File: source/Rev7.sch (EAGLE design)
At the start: 8 parts

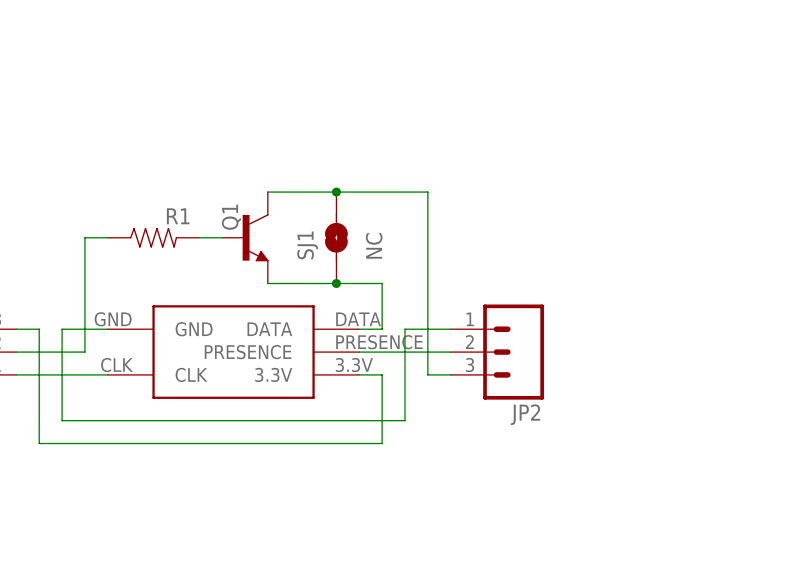
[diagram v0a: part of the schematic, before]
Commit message: Updated Rev7: down to 1 via and much better signal layout. Pin layout has changed
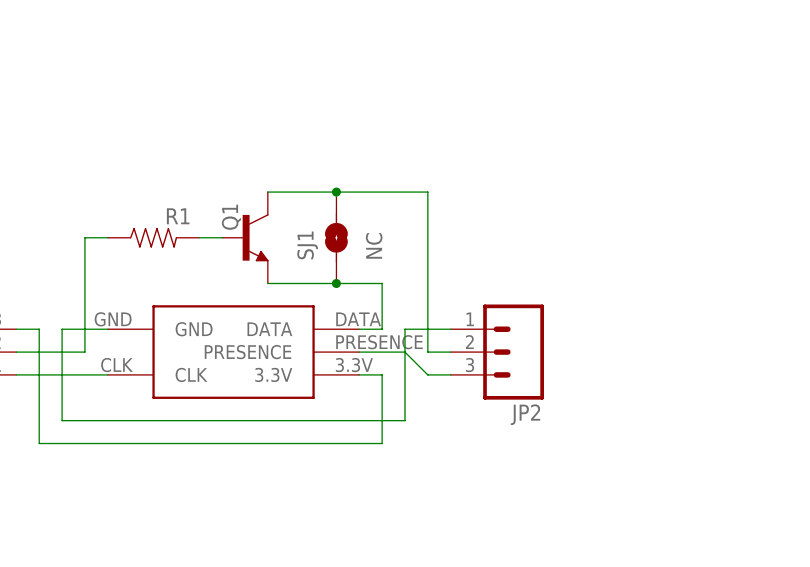
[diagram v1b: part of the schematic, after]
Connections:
- removed net PRES: JP2.2, U$1.PRESENCE
- new net N$2: JP2.3, U$1.PRESENCE
- net N$6: now also JP2.2; no longer JP2.3
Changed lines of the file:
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@@
 </busses>
 <nets>
-<net name="PRES" class="0">
-<segment>
-<pinref part="U$1" gate="G$1" pin="PRESENCE"/>
-<wire x1="157.48" y1="114.3" x2="147.32" y2="114.3" width="0.1524" layer="91"/>
-<pinref part="JP2" gate="G$1" pin="2"/>
-</segment>
-</net>
 <net name="SCL" class="0">
 <segment>
@@
 <wire x1="144.78" y1="132.08" x2="137.16" y2="132.08" width="0.1524" layer="91"/>
 <pinref part="Q1" gate="G$1" pin="C"/>
-<wire x1="154.94" y1="132.08" x2="154.94" y2="111.76" width="0.1524" layer="91"/>
+<pinref part="JP2" gate="G$1" pin="2"/>
+<wire x1="154.94" y1="132.08" x2="154.94" y2="114.3" width="0.1524" layer="91"/>
+<wire x1="154.94" y1="114.3" x2="157.48" y2="114.3" width="0.1524" layer="91"/>
+</segment>
+</net>
+<net name="N$2" class="0">
+<segment>
+<pinref part="U$1" gate="G$1" pin="PRESENCE"/>
+<wire x1="147.32" y1="114.3" x2="152.4" y2="114.3" width="0.1524" layer="91"/>
+<wire x1="152.4" y1="114.3" x2="154.94" y2="111.76" width="0.1524" layer="91"/>
 <pinref part="JP2" gate="G$1" pin="3"/>
 <wire x1="154.94" y1="111.76" x2="157.48" y2="111.76" width="0.1524" layer="91"/>
